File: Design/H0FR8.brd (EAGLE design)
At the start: 60 x 60.6 mm, 43 parts, among them Q1 MMBT3904LT1, U1 STM32G0B1CEU6QFN_B1CEU6_STM-L, U2 T2035H-6GD2PAK_T2550_STM-M, U3 VOT8121AM-VT, U4 TLP184_GR-TPL,SE, U5 V275LA4P, X1 XTALL_CSTCE8M00G52

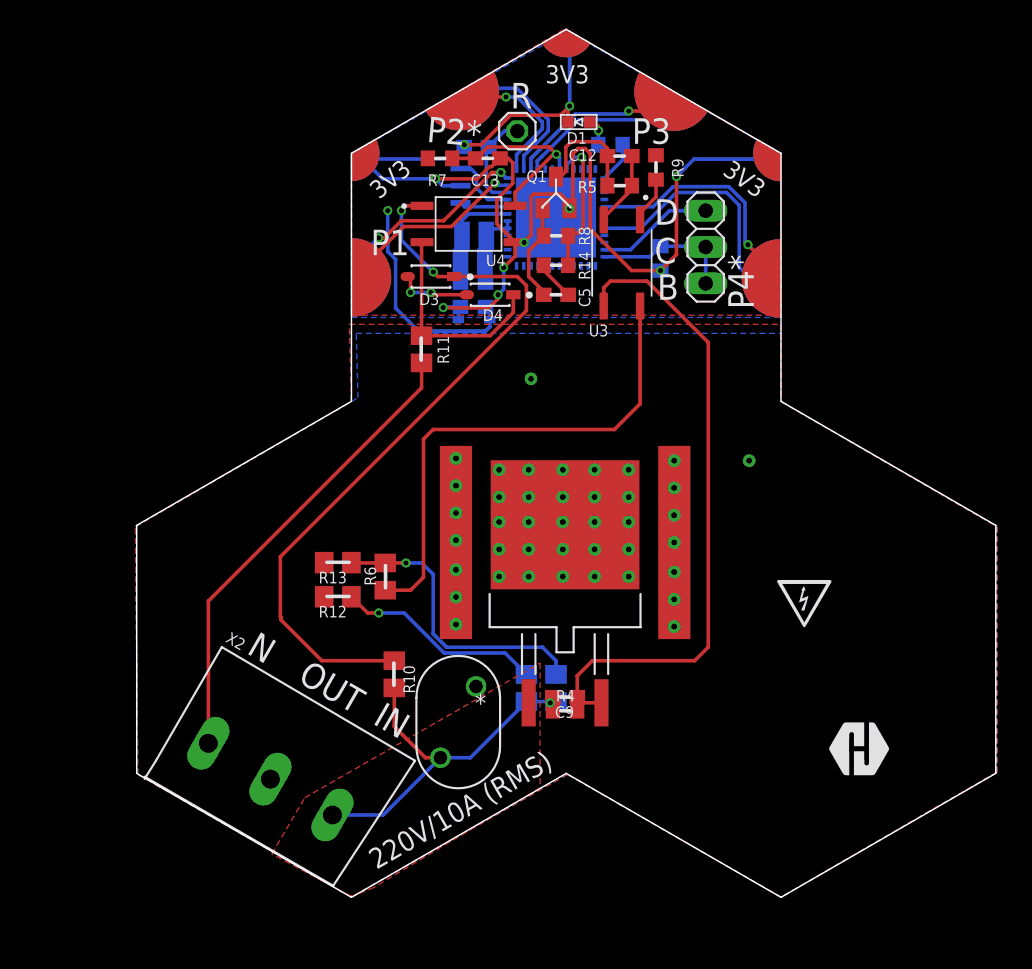
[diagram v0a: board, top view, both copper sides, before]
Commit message: - Changed connector. - Fixed nets. - new pcb layout.
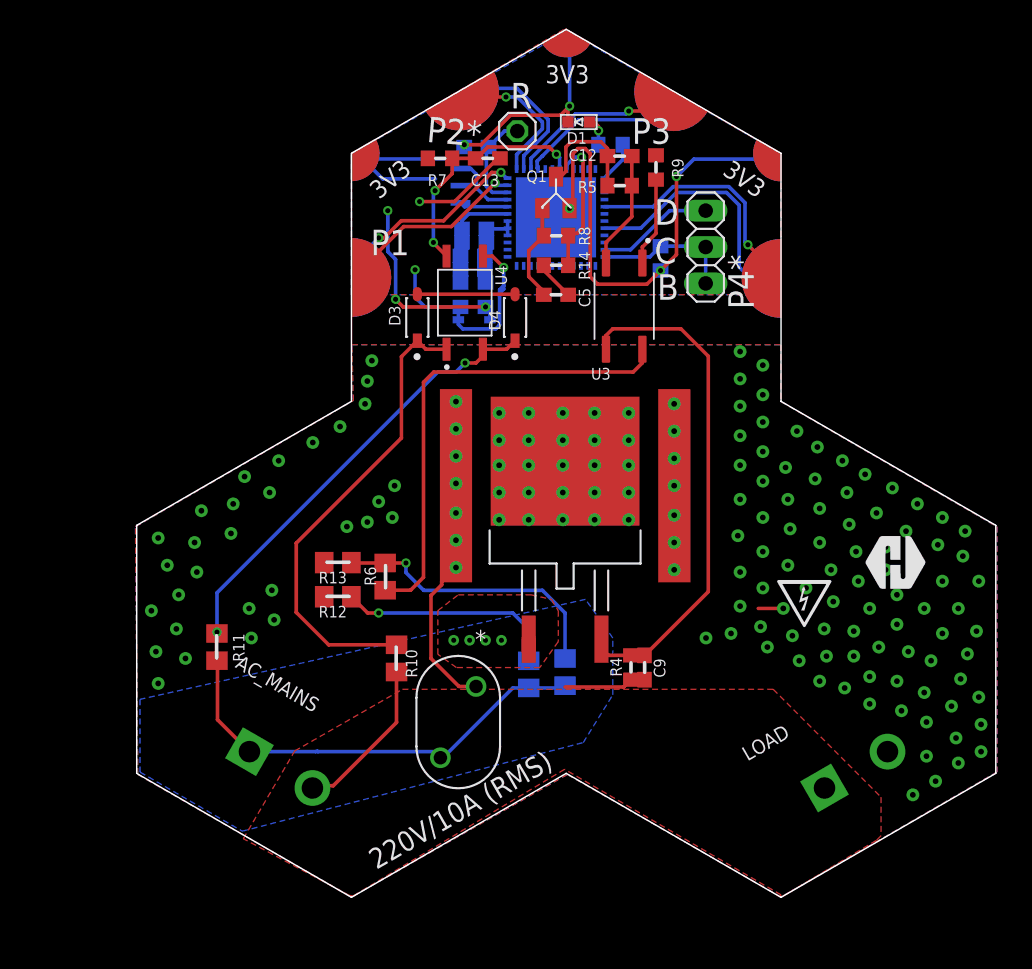
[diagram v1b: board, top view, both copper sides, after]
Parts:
- removed X2: (no value), HEXABITZ_CONNECTION_PARTS:AK300/3
- added AC_MAINS, LOAD: (no value), HEXABITZ_CONNECTION_PARTS:1546111-2
- moved R11 25.2 mm to (-24.3, 8.89)
- moved TRIMBLE-LOGO2 13.3 mm to (23.1, 12.9)
- moved C9 5.93 mm to (5.56, 7.46), turned to 270 degrees
- moved R4 5.50 mm to (4.60, 7.46), turned to 90 degrees
- moved U4 5.50 mm to (-7.01, 32.9), turned to 90 degrees
- moved U2 4.45 mm to (0.00, 19.5)
- moved U$2 3.97 mm to (-7.62, 20.2)
- moved U3 3.02 mm to (4.13, 32.7)
- moved D3 3.01 mm to (-10.3, 31.9), turned to 90 degrees
- moved D4 2.36 mm to (-3.49, 31.9), turned to 90 degrees
- moved C11 1.28 mm to (0.00, 7.14)
- moved R10 1.12 mm to (-11.8, 8.10)
- moved C10 0.97 mm to (-2.54, 6.99)
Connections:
- net A2: now also LOAD.2; no longer X2.2
- net AC_MAINS_L: now also AC_MAINS.2, LOAD.1; no longer C10.2, C11.2, C9.2, R4.1, U2.1, U5.1, X2.3
- net AC_MAINS_N: now also AC_MAINS.1, C10.2, C11.2, C9.2, R4.1, U2.1, U5.1; no longer X2.1
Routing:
- net N$15: track 53.3 -> 32.7 mm, vias 2 -> 0
- net N$16: track 14.9 -> 31.2 mm, vias 0 -> 2
- net AC_MAINS_L: track 27.6 -> 11.3 mm, vias 1 -> 0
- net A2: track 0.00 -> 12.8 mm, vias 41 -> 157
- net TRIAC_G: track 46.1 -> 35.7 mm
- net GND: track 92.6 -> 85.9 mm, vias 10 -> 8
- net AC_MAINS_N: track 32.7 -> 38.9 mm, vias 0 -> 4
- net N$3: track 3.27 -> 6.22 mm
- net N$10: track 5.26 -> 8.21 mm
- net ZC_DETECT: track 13.9 -> 16.7 mm, vias 1 -> 3
- net N$8: track 35.7 -> 33.5 mm
- net VDD: track 15.9 -> 13.9 mm, vias 1 -> 3
- net N$14: track 5.19 -> 6.83 mm, vias 2 -> 0
- net N$4: track 14.5 -> 15.5 mm
- net N$7: track 20.5 -> 19.9 mm
- added copper zone on layer 1, net AC_MAINS_N
- added copper zone on layer 16, net AC_MAINS_N
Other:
- board text removed: "IN"
- board text removed: "N"
- board text removed: "OUT"

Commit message: - Silkscreen is done. - Alligned vias.
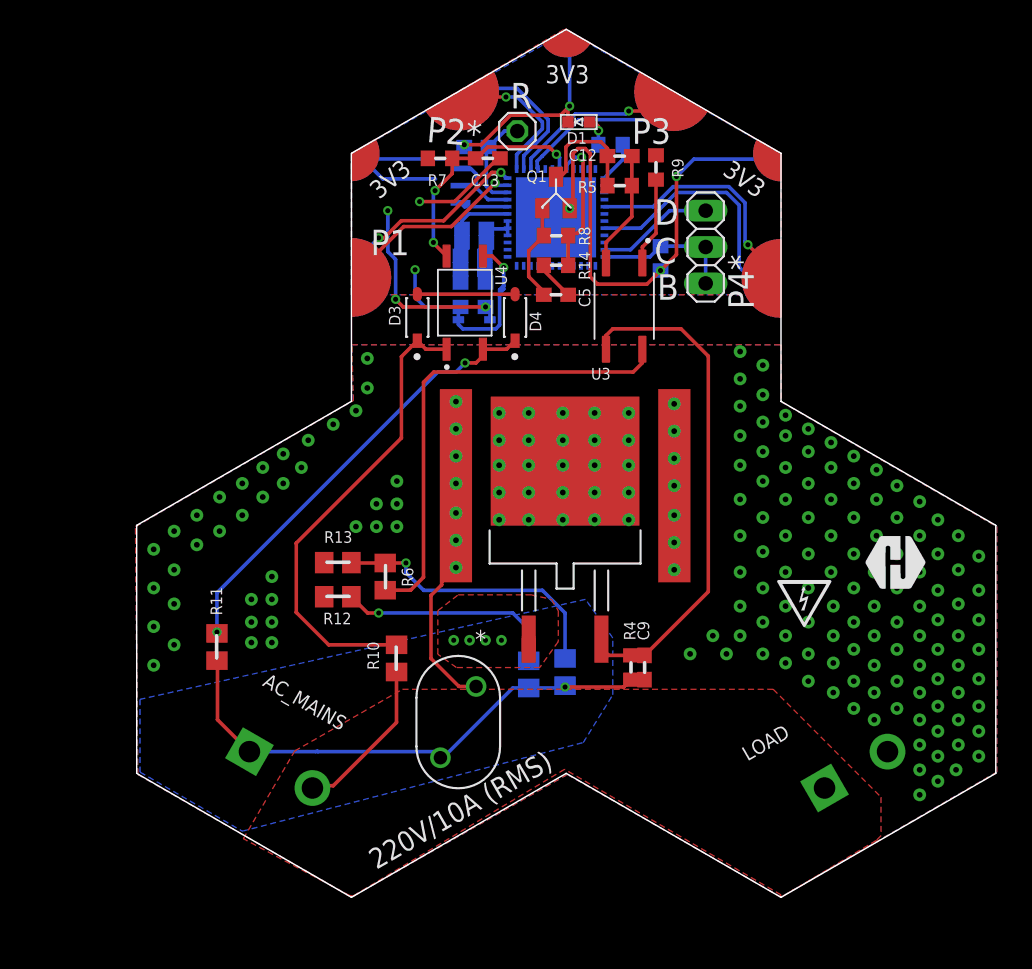
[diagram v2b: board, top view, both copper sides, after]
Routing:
- net A2: track 12.8 -> 11.0 mm, vias 157 -> 190
- net AC_MAINS_N: track 38.9 -> 38.6 mm, vias 4 -> 5

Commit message: - Changed components description in BOM - Fixed issues in Layout - Fixed issues in Schematic - Generated new documentation
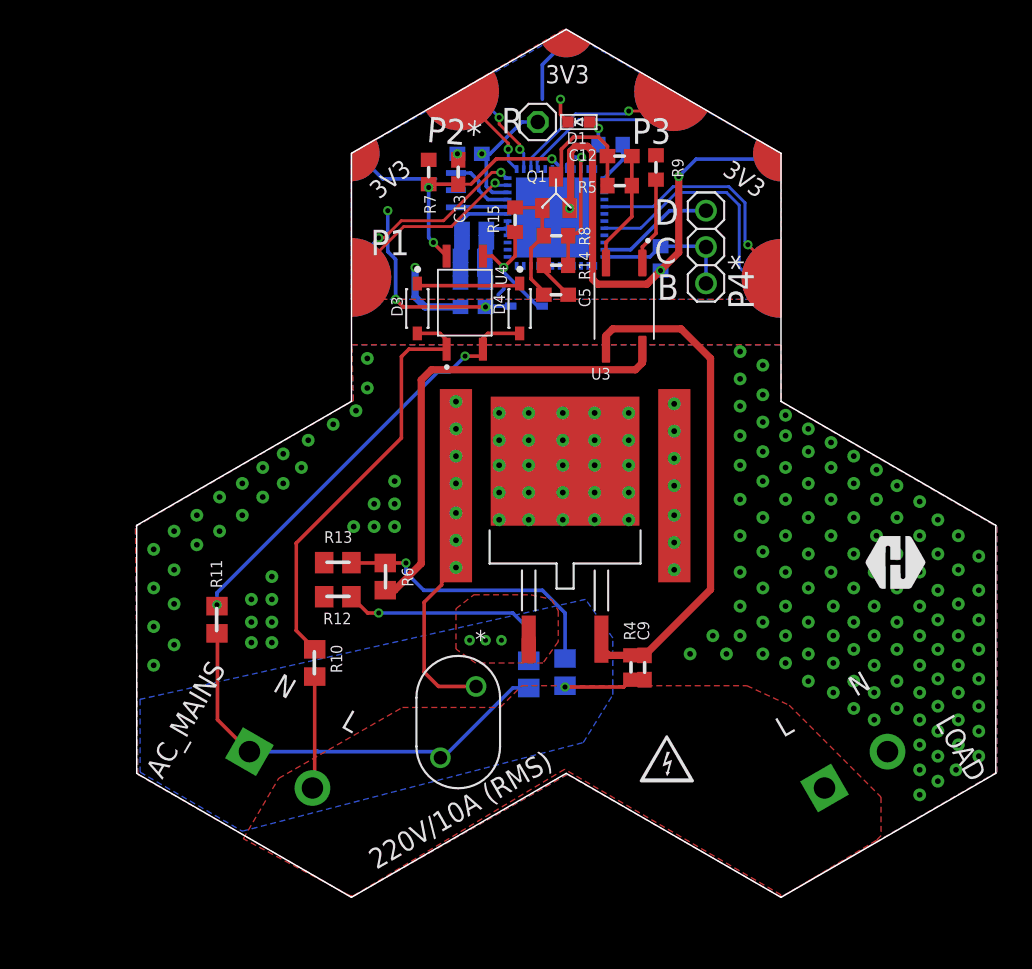
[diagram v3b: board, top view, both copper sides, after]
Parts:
- added R15: 100k, HEXABITZ_RCLS:R-0603
- SWD: device pinhead:1X03 -> HEXABITZ_CONNECTION_PARTS:1X03
- moved R10 5.72 mm to (-17.5, 7.78)
- moved D2 3.77 mm to (-2.70, 32.7), turned to 180 degrees
- moved C13 2.27 mm to (-7.46, 42.1), turned to 90 degrees
- moved R11 1.90 mm to (-24.3, 10.8)
- moved R 1.56 mm to (-1.91, 45.6)
- moved R7 1.24 mm to (-9.53, 42.1), turned to 270 degrees
- moved D4 0.70 mm to (-3.17, 32.5), turned to 270 degrees
- moved C1 0.67 mm to (-6.67, 43.3)
- moved D3 0.63 mm to (-10.3, 32.5), turned to 270 degrees
- moved X1 0.45 mm to (-7.62, 40.8)
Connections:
- net GND: now also R15.2
- net N$13: now also R15.1
- net N$14: now also D3.1, D4.1; no longer D3.2, D4.2
- net N$15: now also D3.2; no longer D3.1
- net N$16: now also D4.2; no longer D4.1
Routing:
- net GND: track 85.9 -> 63.4 mm, vias 8 -> 7
- net USART2_RX: track 11.2 -> 7.25 mm, vias 0 -> 2
- net USART2_TX: track 10.3 -> 6.35 mm
- net AC_MAINS_L: track 11.3 -> 7.85 mm
- net N$15: track 32.7 -> 30.3 mm
- net N$2: track 6.95 -> 8.90 mm, vias 0 -> 1
- net N$13: track 6.96 -> 8.75 mm
- net A2: track 11.0 -> 12.3 mm
- net N$16: track 31.2 -> 30.3 mm
- net AC_MAINS_N: track 38.6 -> 37.7 mm, vias 5 -> 4
- net ZC_DETECT: track 16.7 -> 15.8 mm
- net VDD: track 13.9 -> 14.7 mm
- net N$14: track 6.83 -> 7.44 mm
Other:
- board text added: "L"
- board text added: "N"

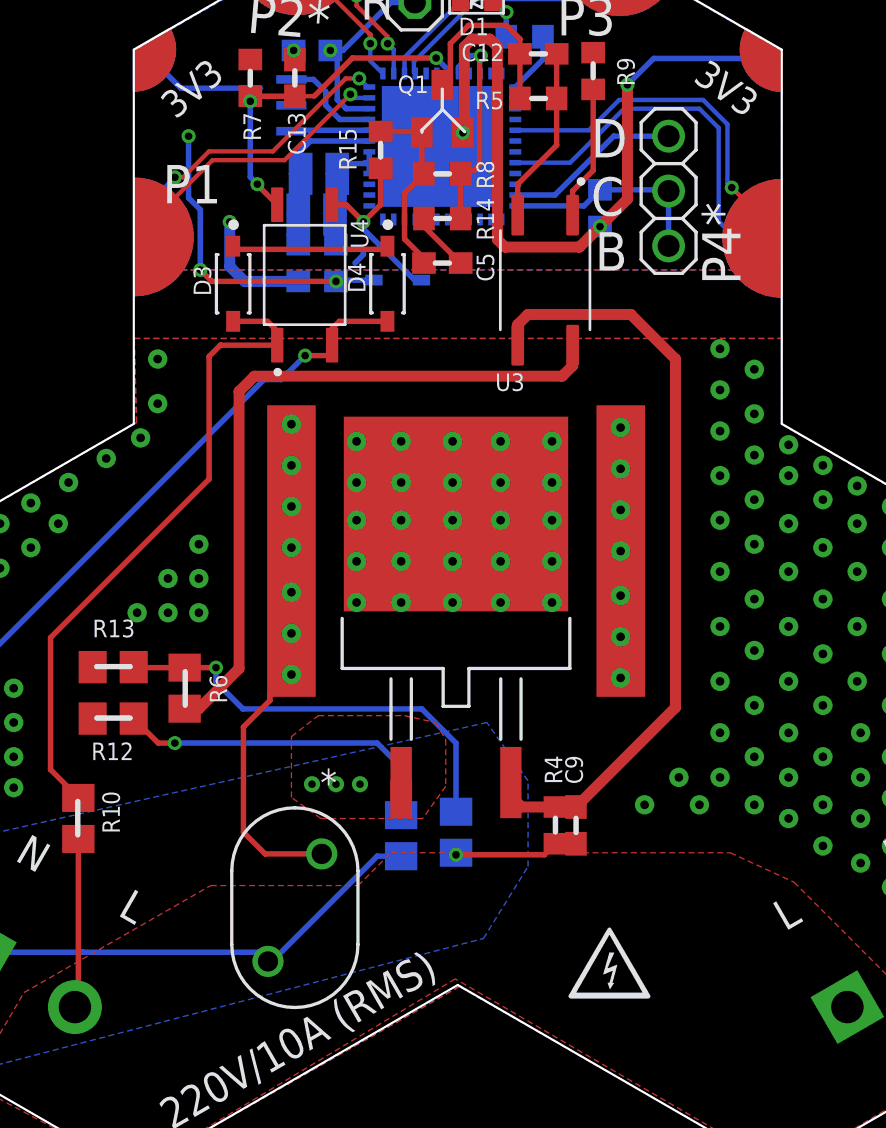
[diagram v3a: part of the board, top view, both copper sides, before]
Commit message: - Changed layout - Rearranged components in BOM
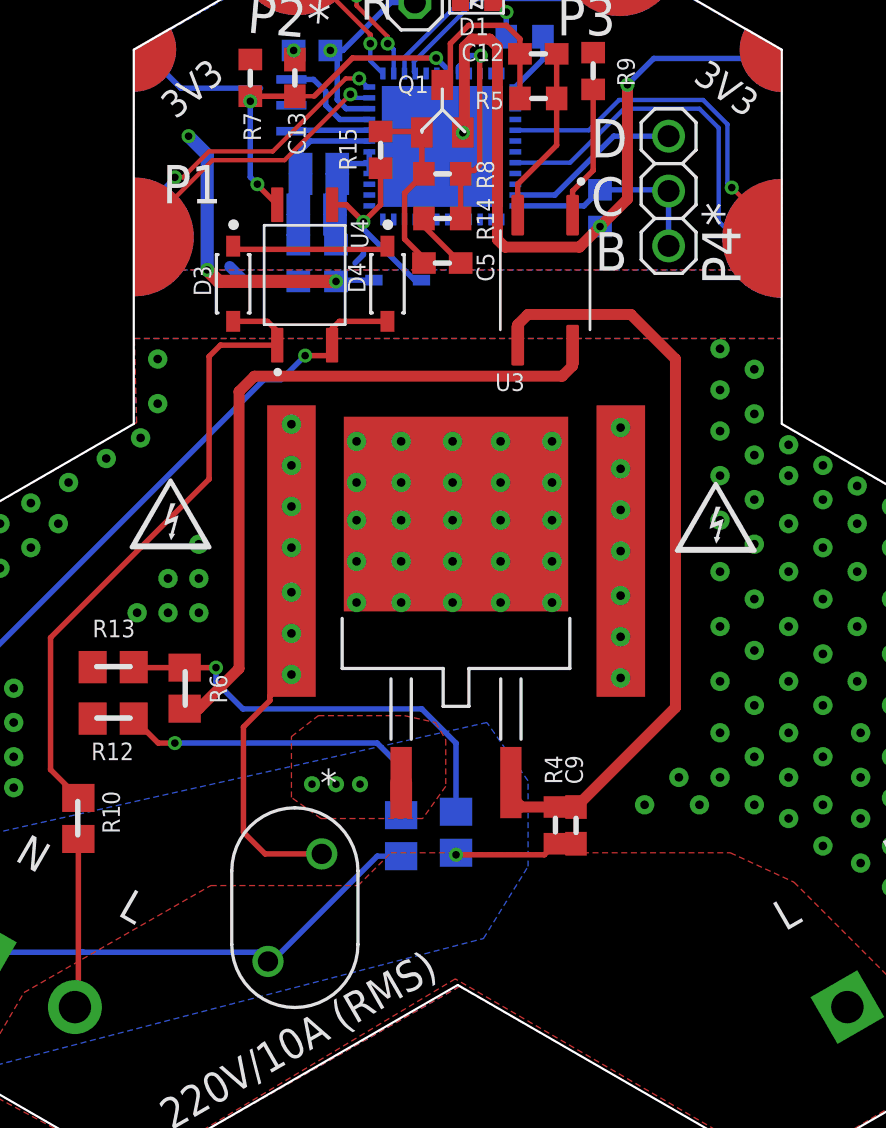
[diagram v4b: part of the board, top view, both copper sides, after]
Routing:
- net GND: track 63.4 -> 61.1 mm, vias 7 -> 6

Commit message: -The final design, all done.
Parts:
- removed D3, D4: STMICROELECTRONICS_BAT46ZFILMSTMICROELECTRONICS_BAT46ZFILM_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, HEXABITZ_RCLS:STMICROELECTRONICS_BAT46ZFILM_3
- removed U2: T2035H-6GD2PAK_T2550_STM-M, HEXABITZ_ICs:D2PAK_T2550_STM-M
- removed U5: V275LA4P, HEXABITZ_RCLS:LA_07MM_LOW_LTF
- added Q2: T2035H-6G, HEXABITZ_ICs:T2035H6G
- added VDR1: V275LA4P, HEXABITZ_RCLS:LA_07MM_LOW_LTF
- added Z1, Z2: MMSZ5225BT1G, HEXABITZ_RCLS:SOD3716X135N
- C2, C3: device HEXABITZ_RCLS:C-0603-POL -> HEXABITZ_RCLS:C-0805-POL
- D1: device Hexabitz:VLMS1300-GS08 -> HEXABITZ_USER_INTERFACE_PARTS:VLMS1300-GS08
- moved R11 23.8 mm to (-8.57, 28.7), flipped to the bottom, turned to 0 degrees
- moved R10 21.4 mm to (-12.9, 28.7), flipped to the bottom, turned to 0 degrees
- moved R13 15.4 mm to (-0.50, 13.5), flipped to the bottom, turned to 90 degrees
- moved R6 14.5 mm to (1.74, 11.8), flipped to the bottom, turned to 0 degrees
- moved R12 13.4 mm to (-2.56, 13.5), flipped to the bottom, turned to 90 degrees
- moved LOAD 12.6 mm to (8.73, -4.60), turned to 180 degrees
- moved TRIMBLE-LOGO2 12.2 mm to (12.3, 7.23)
- moved AC_MAINS 12.0 mm to (-8.91, -4.60), turned to 180 degrees
- moved C5 8.60 mm to (-1.27, 42.1), turned to 90 degrees
- moved R14 8.42 mm to (-0.48, 44.0)
- moved R 8.41 mm to (-9.05, 41.1)
- moved D1 7.49 mm to (7.30, 41.6)
- moved C13 7.27 mm to (-3.65, 35.9), turned to 0 degrees
- moved R7 6.96 mm to (-6.35, 35.9), turned to 0 degrees
- moved C9 6.13 mm to (-0.16, 9.68), turned to 180 degrees
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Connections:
- removed net N$14: D3.1, D4.1
- removed net USART4_RX: U$1.PAD_PD3, U1.12
- removed net USART4_TX: U$1.PAD_PU3, U1.11
- new net N$12: Z1.2, Z2.2
- net A2: now also LOAD.1, Q2.2, VDR1.2; no longer LOAD.2, U2.2, U5.2
- net AC_MAINS_L: now also AC_MAINS.1, LOAD.2; no longer AC_MAINS.2, LOAD.1
- net AC_MAINS_N: now also AC_MAINS.2, Q2.1, VDR1.1; no longer AC_MAINS.1, U2.1, U5.1
- net LED_INDICATOR: now also U1.33; no longer U1.25
- net N$15: now also Z1.1; no longer D3.2
- net N$16: now also Z2.1; no longer D4.2
- net TRIAC_G: now also Q2.3; no longer U2.3
- net TRIAC_TRIGGER: now also U1.17; no longer U1.20
- net USART1_RX: now also U$1.PAD_PD2; no longer U$1.PAD_PD8
- net USART1_TX: now also U$1.PAD_PU2; no longer U$1.PAD_PU8
- net USART5_RX: now also U$1.PAD_PD8
- net USART5_TX: now also U$1.PAD_PU8
- net USART6_RX: now also U$1.PAD_PD3, U1.48; no longer U$1.PAD_PD2, U1.16
- net USART6_TX: now also U$1.PAD_PU3, U1.47; no longer U$1.PAD_PU2, U1.15
- net ZC_DETECT: now also U1.46; no longer U1.19
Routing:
- net AC_MAINS_L: track 7.85 -> 66.9 mm
- net VDD: track 14.5 -> 71.8 mm, vias 3 -> 1
- net GND: track 61.1 -> 20.7 mm, vias 6 -> 12
- net AC_MAINS_N: track 37.7 -> 60.9 mm, vias 4 -> 1
- net N$16: track 30.3 -> 7.31 mm
- net N$15: track 30.3 -> 11.5 mm, vias 0 -> 1
- net N$7: track 19.9 -> 2.69 mm, vias 1 -> 0
- net USART5_TX: track 0.00 -> 15.4 mm, vias 0 -> 1
- net USART5_RX: track 0.00 -> 15.3 mm
- net USART4_RX: track 14.3 -> 0.00 mm, vias 2 -> 0
- net N$4: track 15.5 -> 1.28 mm, vias 1 -> 0
- net USART4_TX: track 13.3 -> 0.00 mm, vias 1 -> 0
- net USART1_TX: track 16.9 -> 5.28 mm
- net USART1_RX: track 17.7 -> 6.88 mm
- net N$14: track 7.44 -> 0.00 mm
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- added copper zone on layer 16, net AC_MAINS_L
- added copper zone on layer 1, net GND
- removed copper zone on layer 1, net AC_MAINS_L
- removed copper zone on layer 16, net AC_MAINS_N
- removed copper zone on layer 1, net VDD
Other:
- outline, holes or cut-outs redrawn
- board text added: "P3*"
- board text added: "P4"
- board text removed: "P3"
- board text removed: "P4*"
